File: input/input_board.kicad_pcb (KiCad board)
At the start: 4 copper layers, 271.6 x 100 mm, 433 parts, among them J1 Sensor, J101 Gain, J102 +IN, J103 -IN, J2 SCKB, J201 Gain, J202 +IN, J203 -IN, J3 Decimate, J301 Gain, J302 +IN, J303 -IN, J4 SCKA, J5 MCLK, J6 SDOB1, P1 my_pcie_8x, Q1 NSS1C300ET4G, Q2 2STD1665T4, Q3 NSS1C300ET4G, U1 DS90LV048, U101 AD8599, U102 LTC2512-24, U104 THS4131, U2 FIN1047, U201 THS4131, U202 AD8599, U203 LTC2512-24, U3 OP27, U301 THS4131, U302 AD8599, U303 LTC2512-24, U4 OPA830, U5 74LVC541A, U6 OPA830, U7 MCP1755S-3302E/DB, U8 NCP1117STAT3G, U9 OPA1679

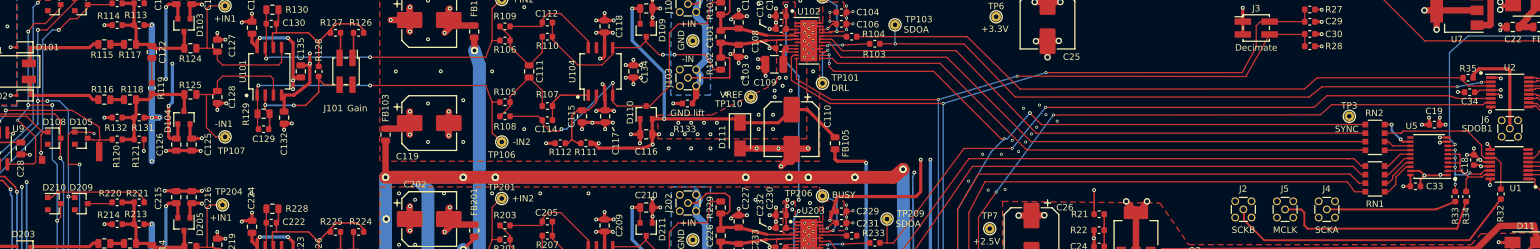
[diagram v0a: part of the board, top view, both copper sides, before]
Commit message: Fixed footprints for U5 and RN1/RN2.  Added gerber files for input board.  Start of work on the main board.
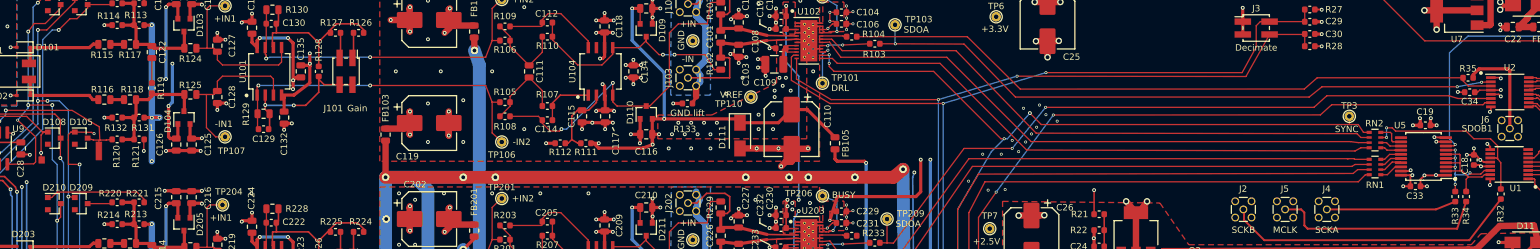
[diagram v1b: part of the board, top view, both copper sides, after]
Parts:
- RN1, RN2: footprint Resistor_SMD:R_Array_Convex_4x1206 -> Resistor_SMD:R_Array_Convex_4x0603
- U5: footprint Package_SO:SSOP-20_4.4x6.5mm_P0.65mm -> input:my-SSOP-20_5.3x7.2mm_P0.65mm
- moved RN1 1.85 mm to (265.5, 81.9)
- moved C19 1.40 mm to (273.4, 75.4)
- moved U5 0.87 mm to (273.1, 80.2)
- moved RN2 0.42 mm to (265.5, 77.7)
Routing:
- net /SCKB_RX: track 25.3 -> 28.9 mm, vias 0 -> 2
- net Net-(RN1-Pad1): track 6.29 -> 3.66 mm
- net Net-(RN1-Pad2): track 5.60 -> 3.68 mm
- net OVDD: track 124.5 -> 126.2 mm, vias 25 -> 26
- net Net-(RN1-Pad3): track 5.07 -> 3.53 mm
- net GND: track 753.2 -> 754.7 mm, vias 417 -> 419
- net Net-(RN1-Pad4): track 4.79 -> 3.47 mm
- net Net-(RN2-Pad4): track 5.65 -> 4.41 mm, vias 2 -> 0
- net Net-(RN2-Pad2): track 4.29 -> 3.37 mm
- net /input_channel/SCKB: track 91.0 -> 91.8 mm
- net Net-(RN2-Pad1): track 4.03 -> 3.31 mm
- net /input_channel/MCLK: track 90.7 -> 91.4 mm
- net SYNC: track 196.8 -> 197.5 mm
- net /input_channel/SCKA: track 91.2 -> 91.8 mm

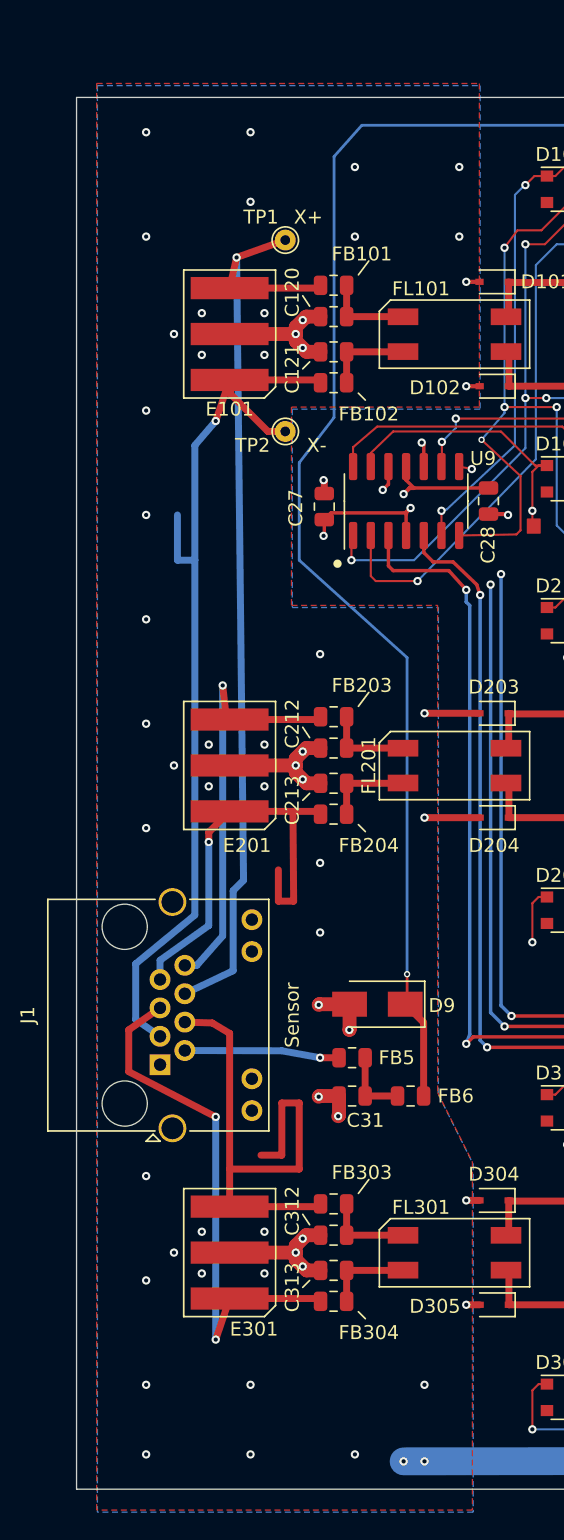
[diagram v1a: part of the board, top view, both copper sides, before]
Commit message: Added mounting holes
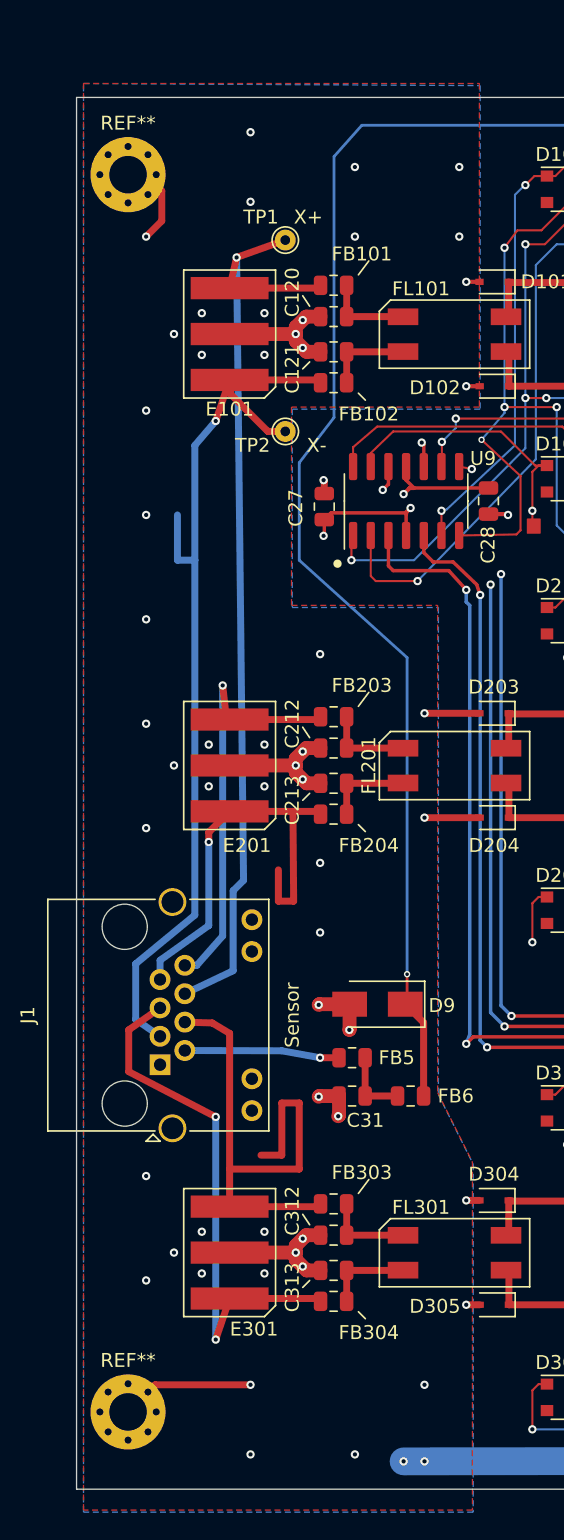
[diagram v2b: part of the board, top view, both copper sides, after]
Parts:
- added REF**: MountingHole_2.7mm_Pad_Via, MountingHole:MountingHole_2.7mm_Pad_Via, F.Cu at (28.7, 144.4)
- added REF**: MountingHole_2.7mm_Pad_Via, MountingHole:MountingHole_2.7mm_Pad_Via, F.Cu at (28.7, 55.5)
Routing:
- net Earth: track 346.4 -> 362.6 mm, vias 63 -> 60
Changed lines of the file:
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@@
   (general
     (thickness 1.6)
-    (drawings 88)
-    (tracks 4098)
+    (drawings 90)
+    (tracks 4101)
     (zones 0)
-    (modules 433)
+    (modules 435)
     (nets 241)
   )
@@
     (45 Margin user hide)
     (46 B.CrtYd user hide)
-    (47 F.CrtYd user)
+    (47 F.CrtYd user hide)
     (48 B.Fab user hide)
     (49 F.Fab user hide)
@@
     (mod_text_size 1 1)
     (mod_text_width 0.18)
-    (pad_size 0.9 0.9)
-    (pad_drill 0)
+    (pad_size 0.8 0.8)
+    (pad_drill 0.5)
     (pad_to_mask_clearance 0.0381)
     (solder_mask_min_width 0.1016)
@@
     (add_net SYNC_IN)
   )
+  (module MountingHole:MountingHole_2.7mm_Pad_Via (layer F.Cu)
+    (at 28.7 144.45)
+    (descr "Mounting Hole 2.7mm")
+    (tags "mounting hole 2.7mm")
+    (attr virtual)
+    (fp_text reference REF** (at 0 -3.7) (layer F.SilkS)
+      (effects (font (size 1 1) (thickness 0.15)))
+    )
+    (fp_text value MountingHole_2.7mm_Pad_Via (at 0 3.7) (layer F.Fab)
+      (effects (font (size 1 1) (thickness 0.15)))
+    )
+    (fp_text user %R (at 0.3 0) (layer F.Fab)
+      (effects (font (size 1 1) (thickness 0.15)))
+    )
+    (fp_circle (center 0 0) (end 2.7 0) (layer Cmts.User) (width 0.15))
+    (fp_circle (center 0 0) (end 2.95 0) (layer F.CrtYd) (width 0.05))
+    (pad 1 thru_hole circle (at 0 0) (size 5.4 5.4) (drill 2.7) (layers *.Cu *.Mask)
+      (net 74 Earth) (zone_connect 2))
+    (pad 1 thru_hole circle (at 2.025 0) (size 0.8 0.8) (drill 0.5) (layers *.Cu *.Mask))
+    (pad 1 thru_hole circle (at 1.431891 1.431891) (size 0.8 0.8) (drill 0.5) (layers *.Cu *.Mask))
+    (pad 1 thru_hole circle (at 0 2.025) (size 0.8 0.8) (drill 0.5) (layers *.Cu *.Mask))
+    (pad 1 thru_hole circle (at -1.431891 1.431891) (size 0.8 0.8) (drill 0.5) (layers *.Cu *.Mask))
+    (pad 1 thru_hole circle (at -2.025 0) (size 0.8 0.8) (drill 0.5) (layers *.Cu *.Mask))
+    (pad 1 thru_hole circle (at -1.431891 -1.431891) (size 0.8 0.8) (drill 0.5) (layers *.Cu *.Mask))
+    (pad 1 thru_hole circle (at 0 -2.025) (size 0.8 0.8) (drill 0.5) (layers *.Cu *.Mask))
+    (pad 1 thru_hole circle (at 1.431891 -1.431891) (size 0.8 0.8) (drill 0.5) (layers *.Cu *.Mask)
+      (net 74 Earth))
+  )
+  (module MountingHole:MountingHole_2.7mm_Pad_Via (layer F.Cu)
+    (at 28.7 55.55)
+    (descr "Mounting Hole 2.7mm")
+    (tags "mounting hole 2.7mm")
+    (attr virtual)
+    (fp_text reference REF** (at 0 -3.7) (layer F.SilkS)
+      (effects (font (size 1 1) (thickness 0.15)))
+    )
+    (fp_text value MountingHole_2.7mm_Pad_Via (at 0 3.7) (layer F.Fab)
+      (effects (font (size 1 1) (thickness 0.15)))
+    )
+    (fp_circle (center 0 0) (end 2.95 0) (layer F.CrtYd) (width 0.05))
+    (fp_circle (center 0 0) (end 2.7 0) (layer Cmts.User) (width 0.15))
+    (fp_text user %R (at 0.3 0) (layer F.Fab)
+      (effects (font (size 1 1) (thickness 0.15)))
+    )
+    (pad 1 thru_hole circle (at 1.431891 -1.431891) (size 0.8 0.8) (drill 0.5) (layers *.Cu *.Mask))
+    (pad 1 thru_hole circle (at 0 -2.025) (size 0.8 0.8) (drill 0.5) (layers *.Cu *.Mask))
+    (pad 1 thru_hole circle (at -1.431891 -1.431891) (size 0.8 0.8) (drill 0.5) (layers *.Cu *.Mask))
+    (pad 1 thru_hole circle (at -2.025 0) (size 0.8 0.8) (drill 0.5) (layers *.Cu *.Mask))
+    (pad 1 thru_hole circle (at -1.431891 1.431891) (size 0.8 0.8) (drill 0.5) (layers *.Cu *.Mask))
+    (pad 1 thru_hole circle (at 0 2.025) (size 0.8 0.8) (drill 0.5) (layers *.Cu *.Mask))
+    (pad 1 thru_hole circle (at 1.431891 1.431891) (size 0.8 0.8) (drill 0.5) (layers *.Cu *.Mask))
+    (pad 1 thru_hole circle (at 2.025 0) (size 0.8 0.8) (drill 0.5) (layers *.Cu *.Mask)
+      (net 74 Earth))
+    (pad 1 thru_hole circle (at 0 0) (size 5.4 5.4) (drill 2.7) (layers *.Cu *.Mask)
+      (net 74 Earth))
+  )
   (module input:my-SSOP-20_5.3x7.2mm_P0.65mm (layer F.Cu)
     (at 273.05 80.25 180)
@@
     )
   )
+  (gr_poly (pts (xy 305.3 110.4) (xy 299.3 110.4) (xy 299.3 58.8) (xy 305.2 58.8)) (layer B.Mask) (width 0.1))
+  (gr_poly (pts (xy 305.3 110.4) (xy 299.3 110.4) (xy 299.3 58.8) (xy 305.2 58.8)) (layer F.Mask) (width 0.1))
   (gr_poly (pts (xy 58.3 81.3) (xy 57.4 81.3) (xy 57.4 80.3) (xy 58.3 80.3)) (layer F.Cu) (width 0.1))
   (gr_poly (pts (xy 67.2 80.8) (xy 66.3 80.8) (xy 66.3 78) (xy 67.2 78)) (layer F.Cu) (width 0.1))
@@
   (via (at 41.25 134) (size 0.6) (drill 0.3) (layers F.Cu B.Cu) (net 74))
   (via (at 34 131.5) (size 0.6) (drill 0.3) (layers F.Cu B.Cu) (net 74))
-  (via (at 30 52.5) (size 0.6) (drill 0.3) (layers F.Cu B.Cu) (net 74))
   (via (at 37.5 52.5) (size 0.6) (drill 0.3) (layers F.Cu B.Cu) (net 74))
   (via (at 45 55) (size 0.6) (drill 0.3) (layers F.Cu B.Cu) (net 74))
@@
   (via (at 30 102.5) (size 0.6) (drill 0.3) (layers F.Cu B.Cu) (net 74))
   (via (at 30 127.5) (size 0.6) (drill 0.3) (layers F.Cu B.Cu) (net 74))
-  (via (at 30 135) (size 0.6) (drill 0.3) (layers F.Cu B.Cu) (net 74))
-  (via (at 30 142.5) (size 0.6) (drill 0.3) (layers F.Cu B.Cu) (net 74))
-  (via (at 30 147.5) (size 0.6) (drill 0.3) (layers F.Cu B.Cu) (net 74))
   (via (at 37.5 147.5) (size 0.6) (drill 0.3) (layers F.Cu B.Cu) (net 74))
   (via (at 45 147.5) (size 0.6) (drill 0.3) (layers F.Cu B.Cu) (net 74))
@@
   (via (at 200.8 147.8) (size 1) (drill 0.6) (layers F.Cu B.Cu) (net 74))
   (segment (start 200.8 145.9875) (end 200.8 147.8) (width 1) (layer F.Cu) (net 74) (status 10))
+  (via (at 30 135) (size 0.6) (drill 0.3) (layers F.Cu B.Cu) (net 74))
+  (segment (start 30.65 142.5) (end 28.7 144.45) (width 0.5) (layer F.Cu) (net 74))
+  (segment (start 37.5 142.5) (end 30.65 142.5) (width 0.5) (layer F.Cu) (net 74))
+  (segment (start 29.958002 55.55) (end 28.7 55.55) (width 0.5) (layer F.Cu) (net 74))
+  (segment (start 31.124999 56.716997) (end 29.958002 55.55) (width 0.5) (layer F.Cu) (net 74))
+  (segment (start 31.124999 58.875001) (end 31.124999 56.716997) (width 0.5) (layer F.Cu) (net 74))
+  (segment (start 30 60) (end 31.124999 58.875001) (width 0.5) (layer F.Cu) (net 74))
   (segment (start 257 117.0625) (end 254.6 117.0625) (width 0.3) (layer F.Cu) (net 75) (status 30))
   (segment (start 301.5 103.5) (end 299.7 103.5) (width 0.15) (layer F.Cu) (net 76) (status 30))
@@
       (pts
         (xy 53.944155 72.25) (xy 40.444155 72.25) (xy 40.444155 86.5) (xy 50.944155 86.5) (xy 50.944155 121.5)
-        (xy 53.444155 126.5) (xy 53.444155 151.5) (xy 26.444155 151.5) (xy 26.444155 49) (xy 53.944155 49)
+        (xy 53.444155 126.5) (xy 53.444155 151.5) (xy 25.5 151.5) (xy 25.5 49) (xy 53.944155 49)
       )
     )
@@
       (pts
         (xy 54 72.400436) (xy 40.5 72.400436) (xy 40.5 86.650436) (xy 51 86.650436) (xy 51 121.650436)
-        (xy 53.5 126.650436) (xy 53.5 151.650436) (xy 26.5 151.650436) (xy 26.5 49.150436) (xy 54 49.150436)
+        (xy 53.5 126.650436) (xy 53.5 151.650436) (xy 25.5 151.650436) (xy 25.5 49) (xy 54 49.150436)
       )
     )

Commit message: Checkpoint of state before I start schematic revisions for the next version of the input board. There are not any substantive modifications to the input board, but some broad changes in component attributes related enabling a fabrication quote.
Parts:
- moved R30 20.3 mm to (273.3, 82.4)
- moved R32 20.3 mm to (264.8, 86.1)
- moved C19 20.3 mm to (253.0, 75.4)
- moved C32 20.3 mm to (180.5, 145.1)
- moved C33 20.3 mm to (251.5, 84.9)
- moved C8 20.3 mm to (230.5, 108.0)
- moved R6 20.3 mm to (224.1, 142.2)
- moved R7 20.3 mm to (224.1, 136.8)
- moved TP110 20.3 mm to (148.0, 71.0)
- moved TP208 20.3 mm to (148.0, 102.0)
- moved TP308 20.3 mm to (148.0, 137.0)
- moved U5 20.3 mm to (252.7, 80.2)
- moved U8 20.3 mm to (208.0, 92.2)
- moved C119 20.3 mm to (97.9, 75.0)
- moved C127 20.3 mm to (64.9, 63.0)
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
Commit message: Add lowpass filter to input board reference buffer, and fix antialias frequency response. Supply and reference testing in notebook.txt, lots of discussion of reference noise.
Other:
- board text added: "CUT"
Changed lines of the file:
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@@
   (general
     (thickness 1.6)
-    (drawings 90)
+    (drawings 102)
     (tracks 4101)
     (zones 0)
@@
     (39 F.Mask user hide)
     (40 Dwgs.User user hide)
-    (41 Cmts.User user hide)
+    (41 Cmts.User user)
     (44 Edge.Cuts user)
     (45 Margin user hide)
@@
     )
   )
+  (gr_line (start 239.9 136.8) (end 239.9 135.9) (layer Cmts.User) (width 0.15))
+  (gr_line (start 238.1 139.3) (end 239.2 142.3) (layer Cmts.User) (width 0.15))
+  (gr_line (start 237 137.5) (end 238.1 139.3) (layer Cmts.User) (width 0.15))
+  (gr_line (start 230.3 139) (end 230.3 137.1) (layer Cmts.User) (width 0.15))
+  (gr_line (start 231 140) (end 230.3 139) (layer Cmts.User) (width 0.15))
+  (gr_line (start 231.8 137.9) (end 231.8 137) (layer Cmts.User) (width 0.15))
+  (gr_line (start 233.5 139.2) (end 231.8 137.9) (layer Cmts.User) (width 0.15))
+  (gr_line (start 248.4 138) (end 247.4 138.6) (layer Cmts.User) (width 0.15))
+  (gr_line (start 248.4 135.8) (end 248.4 138) (layer Cmts.User) (width 0.15))
+  (gr_line (start 238.8 137.7) (end 239.9 136.9) (layer Cmts.User) (width 0.15))
+  (gr_text CUT (at 235.7 139.2) (layer Cmts.User)
+    (effects (font (size 0.762 0.762) (thickness 0.127)))
+  )
+  (gr_text CUT (at 240.5 141.5) (layer Cmts.User)
+    (effects (font (size 0.762 0.762) (thickness 0.127)))
+  )
   (gr_poly (pts (xy 284.98 110.4) (xy 278.98 110.4) (xy 278.98 58.8) (xy 284.88 58.8)) (layer B.Mask) (width 0.1))

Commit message: ~CARDSEL and config memory added to input board schematic, but not yet to the PCB.  ~CARDSEL is now active low (before it was unimplemented).
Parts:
- removed D12, D13, D14, D6, D7: BAS21S, Package_TO_SOT_SMD:SOT-23
- added C41: 10nF, Capacitor_SMD:C_0805_2012Metric, F.Cu at (232.6, 135.4)
- added C42: 3.3 uF, Capacitor_THT:C_Rect_L13.0mm_W6.0mm_P10.00mm_FKS3_FKP3_MKS4, F.Cu at (254.5, 140.6)
- added FB7: 2K Ohm, Inductor_SMD:L_0805_2012Metric, F.Cu at (229.5, 118.0)
- added R37: 3.3K, Resistor_SMD:R_0603_1608Metric, F.Cu at (246.4, 139.2)
- added R38: 0, Resistor_SMD:R_0603_1608Metric, F.Cu at (201.2, 99.5)
- C111, C203, C303: value 33nF -> 10 nF
- C129, C130, C221, C222, C321, C322: value 2.2nF -> 10nF; footprint Capacitor_SMD:C_0603_1608Metric -> Capacitor_SMD:C_0805_2012Metric
- D3, D5: value BAS21S -> 10V (standoff); footprint Package_TO_SOT_SMD:SOT-23 -> Diode_SMD:D_SMA
- FB1, FB2, FB3, FB4: value 21 Ohm -> 180 Ohm
- R36: value 499 -> 2K; footprint Resistor_SMD:R_0805_2012Metric -> Resistor_SMD:R_0603_1608Metric
- U101, U104, U201, U202, U301, U302: footprint Package_SO:SO-8_5.3x6.2mm_P1.27mm -> Package_SO:SOIC-8_3.9x4.9mm_P1.27mm
- U3: value OP27 -> OPA2210
- moved D5 67.4 mm to (188.3, 144.4)
- moved D3 46.0 mm to (188.3, 139.9)
- moved R14 19.5 mm to (222.5, 133.5), turned to 0 degrees
- moved R36 17.7 mm to (234.6, 135.6)
- moved R2 8.34 mm to (230.6, 135.6)
- moved R1 6.91 mm to (230.6, 139.0)
- moved C2 6.00 mm to (227.7, 142.2)
- moved D1 6.00 mm to (222.4, 143.2)
- moved D2 6.00 mm to (222.4, 139.0)
- moved Q1 6.00 mm to (211.1, 139.3)
- moved R4 6.00 mm to (227.7, 138.4)
- moved R6 6.00 mm to (218.1, 142.2)
- moved R7 6.00 mm to (218.1, 136.8)
- moved R5 5.94 mm to (222.5, 135.8)
- moved R3 5.63 mm to (233.6, 142.6)
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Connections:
- C1 pad 2: /reference_buffer/U3+ -> /reference_buffer/U3A+
- C10 pad 2: /power/U6V- -> LPF_-6V
- C11 pad 2: /power/U6V- -> LPF_-6V
- C111 pad 1: /input_channel/antialias_driver/FILTER+ -> /input_channel/antialias_driver/FILTER-
- C111 pad 2: /input_channel/antialias_driver/FILTER- -> /input_channel/antialias_driver/FILTER+
- C2 pad 1: /reference_buffer/U3- -> /reference_buffer/U3B-
- C203 pad 1: /channel2/antialias_driver/FILTER+ -> /channel2/antialias_driver/FILTER-
- C203 pad 2: /channel2/antialias_driver/FILTER- -> /channel2/antialias_driver/FILTER+
- C3 pad 2: /reference_buffer/U3V+ -> LPF_+10V
- C303 pad 1: /channel3/antialias_driver/FILTER+ -> /channel3/antialias_driver/FILTER-
- C303 pad 2: /channel3/antialias_driver/FILTER- -> /channel3/antialias_driver/FILTER+
- C32 pad 1: Earth -> GND
- C32 pad 2: GND -> Earth
- C4 pad 2: /reference_buffer/U3V- -> LPF_-6V
- C7 pad 1: /power/U4V+ -> LPF_+10V
- C8 pad 2: /power/U4V+ -> LPF_+10V
- D1 pad 3: /reference_buffer/U3OUT -> /reference_buffer/U3BOUT
- D2 pad 2: /reference_buffer/U3OUT -> /reference_buffer/U3BOUT
- D3 pad 1: /power/U6V+ -> Earth
- D5 pad 1: V+ -> GND
- D5 pad 2: (no net) -> Earth
- Q1 pad 1: /reference_buffer/U3OUT -> /reference_buffer/U3BOUT
- R1 pad 1: /reference_buffer/U3+ -> /reference_buffer/U3A+
- R14 pad 1: /power/U6V+ -> Net-(C2-Pad2)
- R14 pad 2: Net-(R14-Pad2) -> FILT_+10V
- R15 pad 2: /power/U4V+ -> LPF_+10V
- R16 pad 1: /power/U6V- -> FILT_-6V
- R16 pad 2: FILT_-6V -> LPF_-6V
- R2 pad 1: /reference_buffer/U3- -> /reference_buffer/U3A-
- R3 pad 1: /reference_buffer/U3+ -> /reference_buffer/U3A+
- R3 pad 2: GND -> /reference_buffer/VREF_GROUND_SENSE
- R36 pad 1: Net-(R14-Pad2) -> /reference_buffer/U3AOUT
- R36 pad 2: FILT_+10V -> /reference_buffer/U3A-
- R4 pad 2: /reference_buffer/U3- -> /reference_buffer/U3B-
- R5 pad 2: V+ -> FILT_+10V
- U3 pad 1: (no net) -> /reference_buffer/U3AOUT
- U3 pad 2: /reference_buffer/U3- -> /reference_buffer/U3A+
- U3 pad 3: /reference_buffer/U3+ -> /reference_buffer/U3A-
- U3 pad 4: /reference_buffer/U3V- -> LPF_-6V
- U3 pad 5: (no net) -> /reference_buffer/U3B+
- U3 pad 6: /reference_buffer/U3OUT -> /reference_buffer/U3B-
- U3 pad 7: /reference_buffer/U3V+ -> /reference_buffer/U3BOUT
- U3 pad 8: (no net) -> LPF_+10V
- U4 pad 7: /power/U4V+ -> LPF_+10V
- U6 pad 4: /power/U6V- -> LPF_-6V
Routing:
- net /reference_buffer/VREF_GROUND_SENSE: track 0.00 -> 105.0 mm, vias 0 -> 2
- net V+: track 557.3 -> 480.3 mm, vias 23 -> 20
- net LPF_+10V: track 0.00 -> 71.4 mm, vias 0 -> 2
- net V-: track 447.2 -> 383.4 mm, vias 19 -> 17
- net LPF_-6V: track 0.00 -> 54.2 mm, vias 0 -> 2
- net /reference_buffer/U3BOUT: track 0.00 -> 51.5 mm, vias 0 -> 2
- net /reference_buffer/U3OUT: track 43.8 -> 0.00 mm, vias 3 -> 0
- net VDD: track 148.8 -> 181.6 mm, vias 13 -> 15
- net /power/U4V+: track 27.1 -> 0.00 mm
- net /power/U6V-: track 25.3 -> 0.00 mm
- net /reference_buffer/U3B+: track 0.00 -> 20.7 mm
- net /reference_buffer/U3B-: track 0.00 -> 17.8 mm, vias 0 -> 2
- net /reference_buffer/U3AOUT: track 0.00 -> 17.6 mm, vias 0 -> 2
- net /reference_buffer/U3+: track 14.5 -> 0.00 mm, vias 2 -> 0
- net /reference_buffer/U3A+: track 0.00 -> 13.9 mm, vias 0 -> 2
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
